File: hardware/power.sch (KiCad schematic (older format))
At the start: 14 parts

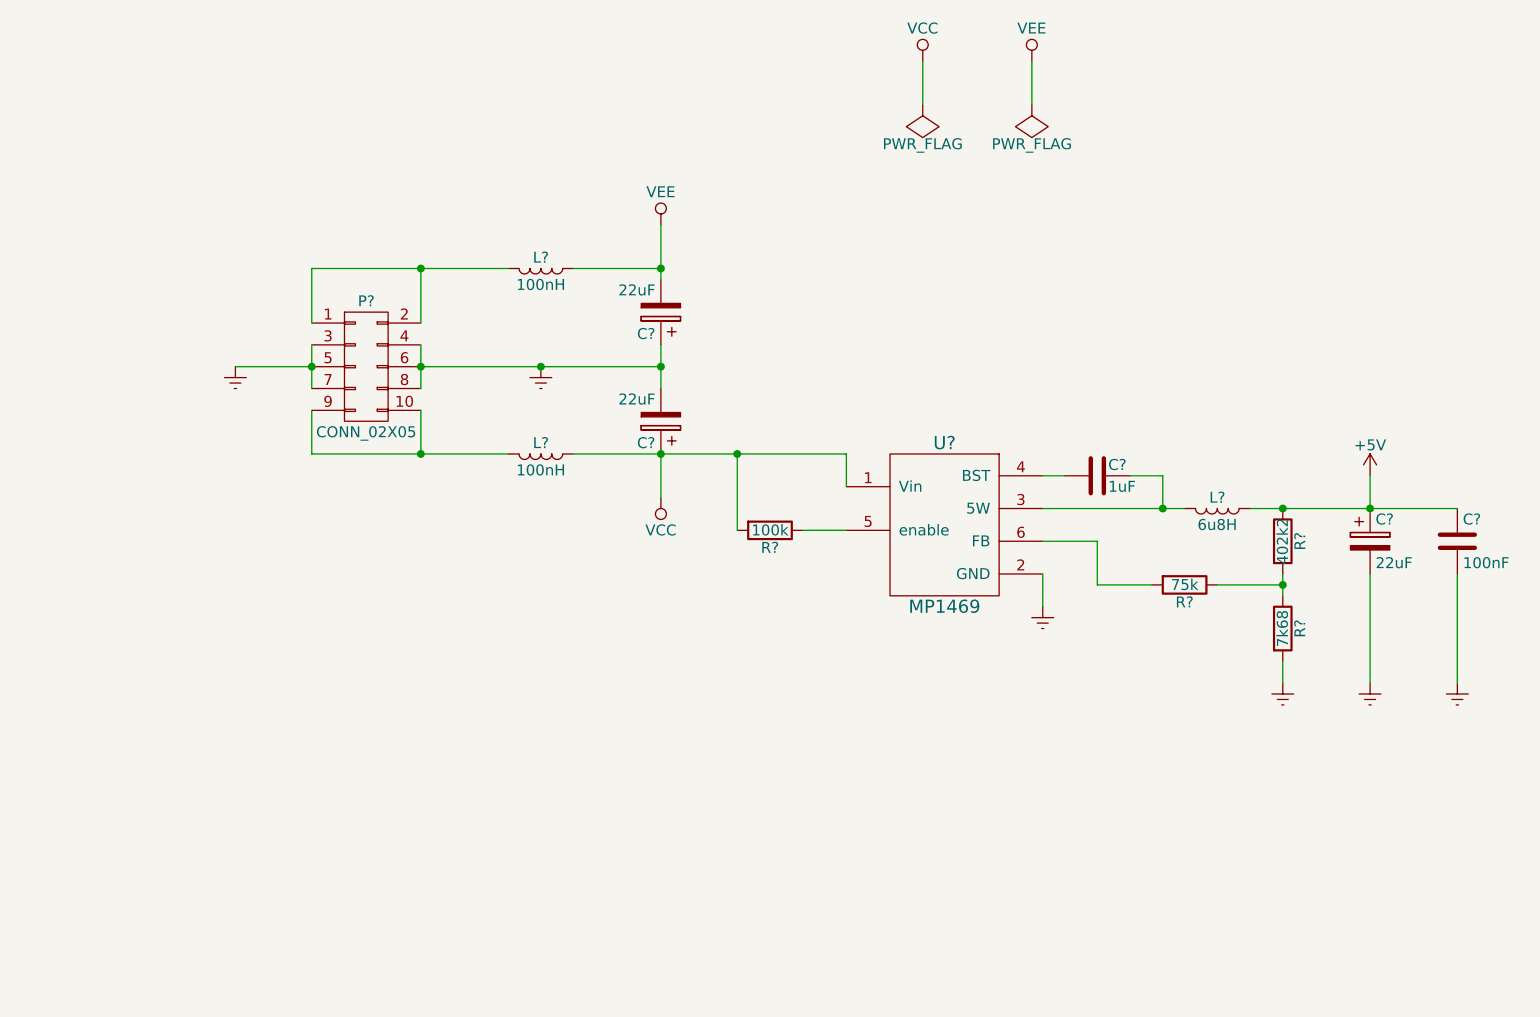
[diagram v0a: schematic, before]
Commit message: jacks on a different sheet than the buffers. single PCB with jumpers and mouse bites
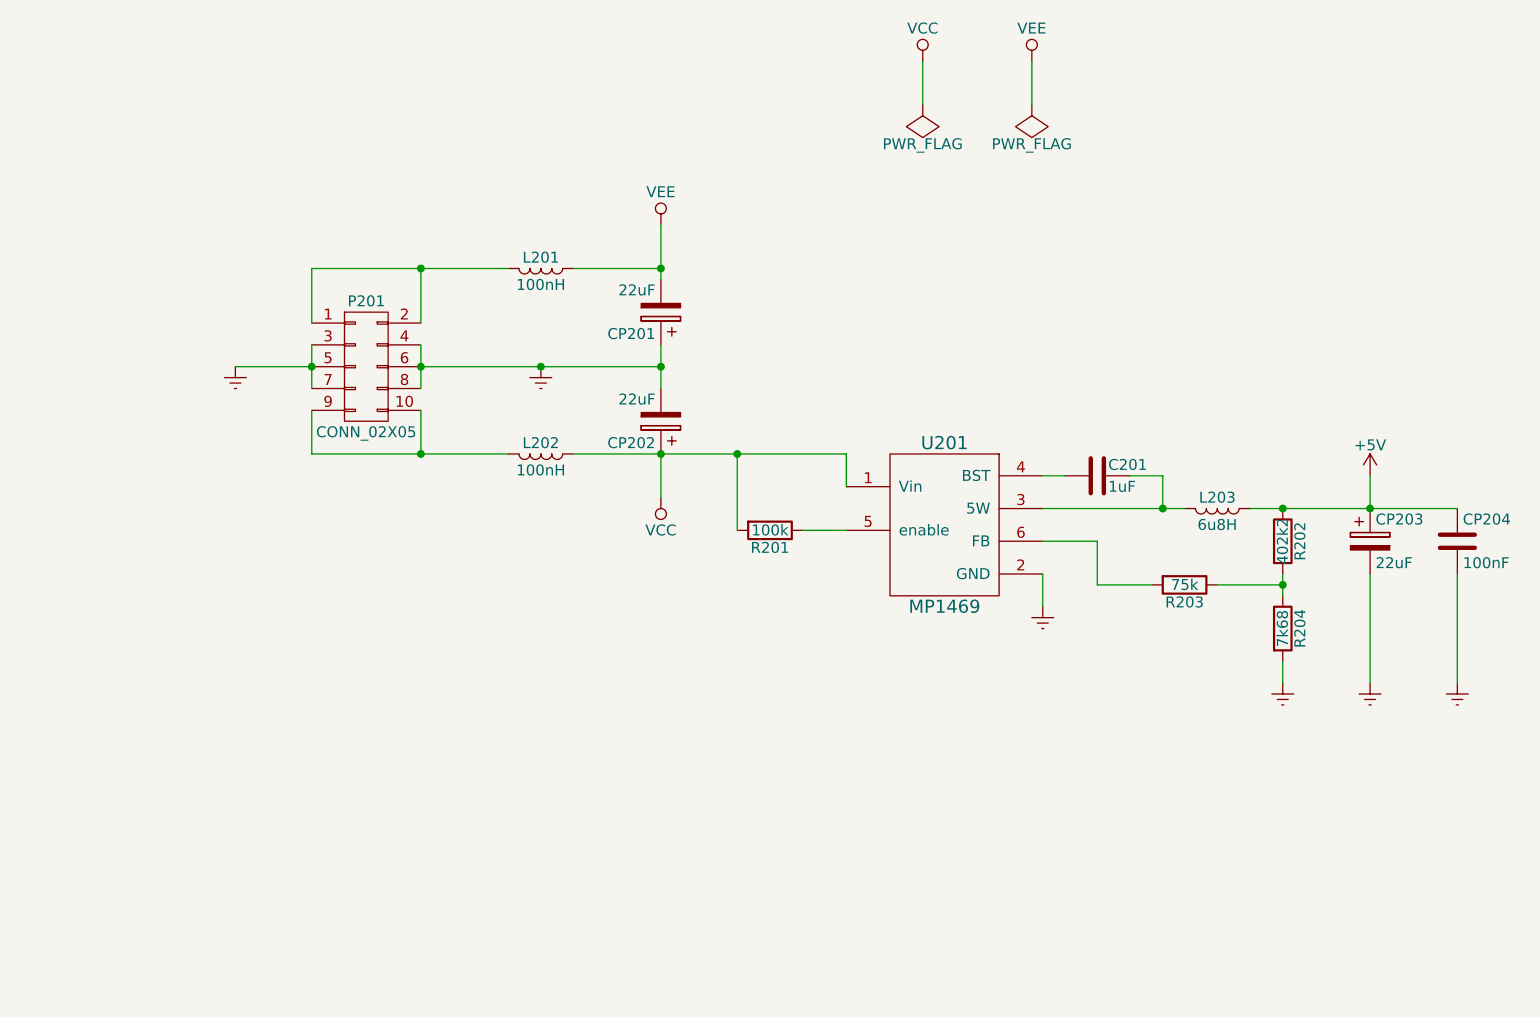
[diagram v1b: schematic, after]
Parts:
- gave numbers to parts that had none: 14
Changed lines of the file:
@@
 $Descr A4 11693 8268
 encoding utf-8
-Sheet 2 4
+Sheet 2 6
 Title ""
 Date ""
@@
 $EndDescr
 $Comp
-L CP C?
+L CP CP201
 U 1 1 5BE1E2D2
 P 4950 2250
-F 0 "C?" H 4975 2350 50  0000 L CNN
+F 0 "CP201" H 4975 2350 50  0000 L CNN
 F 1 "22uF" H 4975 2150 50  0000 L CNN
-F 2 "" H 4988 2100 50  0000 C CNN
+F 2 "" H 4988 2100 50  0001 C CNN
 F 3 "" H 4950 2250 50  0000 C CNN
 	1    4950 2250
@@
 $EndComp
 $Comp
-L CP C?
+L CP CP202
 U 1 1 5BE1E2F6
 P 4950 2750
-F 0 "C?" H 4975 2850 50  0000 L CNN
+F 0 "CP202" H 4975 2850 50  0000 L CNN
 F 1 "22uF" H 4975 2650 50  0000 L CNN
-F 2 "" H 4988 2600 50  0000 C CNN
+F 2 "" H 4988 2600 50  0001 C CNN
 F 3 "" H 4950 2750 50  0000 C CNN
 	1    4950 2750
@@
 $EndComp
 $Comp
-L R R?
+L R R201
 U 1 1 5BE1E3E6
 P 5450 3250
-F 0 "R?" V 5530 3250 50  0000 C CNN
+F 0 "R201" V 5530 3250 50  0000 C CNN
 F 1 "100k" V 5450 3250 50  0000 C CNN
-F 2 "" V 5380 3250 50  0000 C CNN
+F 2 "" V 5380 3250 50  0001 C CNN
 F 3 "" H 5450 3250 50  0000 C CNN
 	1    5450 3250
@@
 	4950 1850 4950 2100
 $Comp
-L L L?
+L L L201
 U 1 1 5BE1E5E0
 P 4400 2050
-F 0 "L?" V 4350 2050 50  0000 C CNN
+F 0 "L201" V 4350 2050 50  0000 C CNN
 F 1 "100nH" V 4475 2050 50  0000 C CNN
-F 2 "" H 4400 2050 50  0000 C CNN
+F 2 "" H 4400 2050 50  0001 C CNN
 F 3 "" H 4400 2050 50  0000 C CNN
 	1    4400 2050
@@
 $EndComp
 $Comp
-L L L?
+L L L202
 U 1 1 5BE1E717
 P 4400 2900
-F 0 "L?" V 4350 2900 50  0000 C CNN
+F 0 "L202" V 4350 2900 50  0000 C CNN
 F 1 "100nH" V 4475 2900 50  0000 C CNN
-F 2 "" H 4400 2900 50  0000 C CNN
+F 2 "" H 4400 2900 50  0001 C CNN
 F 3 "" H 4400 2900 50  0000 C CNN
 	1    4400 2900
@@
 	4550 2900 5800 2900
 $Comp
-L L L?
+L L L203
 U 1 1 5BE1E8D0
 P 7500 3150
-F 0 "L?" V 7450 3150 50  0000 C CNN
+F 0 "L203" V 7450 3150 50  0000 C CNN
 F 1 "6u8H" V 7575 3150 50  0000 C CNN
-F 2 "" H 7500 3150 50  0000 C CNN
+F 2 "" H 7500 3150 50  0001 C CNN
 F 3 "" H 7500 3150 50  0000 C CNN
 	1    7500 3150
@@
 $EndComp
 $Comp
-L MP1469 U?
+L MP1469 U201
 U 1 1 5BE1ECAF
 P 6250 3250
-F 0 "U?" H 6250 3650 60  0000 C CNN
+F 0 "U201" H 6250 3650 60  0000 C CNN
 F 1 "MP1469" H 6250 2900 60  0000 C CNN
 F 2 "" H 6100 3150 60  0001 C CNN
@@
 Connection ~ 5300 2900
 $Comp
-L C C?
+L C C201
 U 1 1 5BE1EF8F
 P 6950 3000
-F 0 "C?" V 6900 3050 50  0000 L CNN
+F 0 "C201" V 6900 3050 50  0000 L CNN
 F 1 "1uF" V 7000 3050 50  0000 L CNN
-F 2 "" H 6988 2850 50  0000 C CNN
+F 2 "" H 6988 2850 50  0001 C CNN
 F 3 "" H 6950 3000 50  0000 C CNN
 	1    6950 3000
@@
 	7100 3000 7250 3000
 $Comp
-L Earth #PWR?
+L Earth #PWR08
 U 1 1 5BE1F1F6
 P 6700 3600
-F 0 "#PWR?" H 6700 3350 50  0001 C CNN
+F 0 "#PWR08" H 6700 3350 50  0001 C CNN
 F 1 "Earth" H 6700 3450 50  0001 C CNN
 F 2 "" H 6700 3600 50  0000 C CNN
@@
 	6700 3450 6700 3600
 $Comp
-L R R?
+L R R203
 U 1 1 5BE1F26C
 P 7350 3500
-F 0 "R?" V 7430 3500 50  0000 C CNN
+F 0 "R203" V 7430 3500 50  0000 C CNN
 F 1 "75k" V 7350 3500 50  0000 C CNN
-F 2 "" V 7280 3500 50  0000 C CNN
+F 2 "" V 7280 3500 50  0001 C CNN
 F 3 "" H 7350 3500 50  0000 C CNN
 	1    7350 3500
@@
 	6700 3300 6950 3300
 $Comp
-L CP C?
+L CP CP203
 U 1 1 5BE1F3E4
 P 8200 3300
-F 0 "C?" H 8225 3400 50  0000 L CNN
+F 0 "CP203" H 8225 3400 50  0000 L CNN
 F 1 "22uF" H 8225 3200 50  0000 L CNN
-F 2 "" H 8238 3150 50  0000 C CNN
+F 2 "" H 8238 3150 50  0001 C CNN
 F 3 "" H 8200 3300 50  0000 C CNN
 	1    8200 3300
@@
 $EndComp
 $Comp
-L +5V #PWR?
+L +5V #PWR09
 U 1 1 5BE1F4C6
 P 8200 3000
-F 0 "#PWR?" H 8200 2850 50  0001 C CNN
+F 0 "#PWR09" H 8200 2850 50  0001 C CNN
 F 1 "+5V" H 8200 3140 50  0000 C CNN
 F 2 "" H 8200 3000 50  0000 C CNN
@@
 $EndComp
 $Comp
-L R R?
+L R R204
 U 1 1 5BE1F506
 P 7800 3700
-F 0 "R?" V 7880 3700 50  0000 C CNN
+F 0 "R204" V 7880 3700 50  0000 C CNN
 F 1 "7k68" V 7800 3700 50  0000 C CNN
-F 2 "" V 7730 3700 50  0000 C CNN
+F 2 "" V 7730 3700 50  0001 C CNN
 F 3 "" H 7800 3700 50  0000 C CNN
 	1    7800 3700
@@
 $EndComp
 $Comp
-L R R?
+L R R202
 U 1 1 5BE1F574
 P 7800 3300
-F 0 "R?" V 7880 3300 50  0000 C CNN
+F 0 "R202" V 7880 3300 50  0000 C CNN
 F 1 "402k2" V 7800 3300 50  0000 C CNN
-F 2 "" V 7730 3300 50  0000 C CNN
+F 2 "" V 7730 3300 50  0001 C CNN
 F 3 "" H 7800 3300 50  0000 C CNN
 	1    7800 3300
@@
 Connection ~ 8200 3150
 $Comp
-L C C?
+L C CP204
 U 1 1 5BE1F870
 P 8600 3300
-F 0 "C?" H 8625 3400 50  0000 L CNN
+F 0 "CP204" H 8625 3400 50  0000 L CNN
 F 1 "100nF" H 8625 3200 50  0000 L CNN
-F 2 "" H 8638 3150 50  0000 C CNN
+F 2 "" H 8638 3150 50  0001 C CNN
 F 3 "" H 8600 3300 50  0000 C CNN
 	1    8600 3300
@@
 $EndComp
 $Comp
-L Earth #PWR?
+L Earth #PWR010
 U 1 1 5BE1F909
 P 7800 3950
-F 0 "#PWR?" H 7800 3700 50  0001 C CNN
+F 0 "#PWR010" H 7800 3700 50  0001 C CNN
 F 1 "Earth" H 7800 3800 50  0001 C CNN
 F 2 "" H 7800 3950 50  0000 C CNN
@@
 $EndComp
 $Comp
-L Earth #PWR?
+L Earth #PWR011
 U 1 1 5BE1F942
 P 8200 3950
-F 0 "#PWR?" H 8200 3700 50  0001 C CNN
+F 0 "#PWR011" H 8200 3700 50  0001 C CNN
 F 1 "Earth" H 8200 3800 50  0001 C CNN
 F 2 "" H 8200 3950 50  0000 C CNN
@@
 $EndComp
 $Comp
-L Earth #PWR?
+L Earth #PWR012
 U 1 1 5BE1F974
 P 8600 3950
-F 0 "#PWR?" H 8600 3700 50  0001 C CNN
+F 0 "#PWR012" H 8600 3700 50  0001 C CNN
 F 1 "Earth" H 8600 3800 50  0001 C CNN
 F 2 "" H 8600 3950 50  0000 C CNN
@@
 	6950 3500 7200 3500
 $Comp
-L CONN_02X05 P?
+L CONN_02X05 P201
 U 1 1 5BE200D6
 P 3600 2500
-F 0 "P?" H 3600 2800 50  0000 C CNN
+F 0 "P201" H 3600 2800 50  0000 C CNN
 F 1 "CONN_02X05" H 3600 2200 50  0000 C CNN
-F 2 "" H 3600 1300 50  0000 C CNN
+F 2 "" H 3600 1300 50  0001 C CNN
 F 3 "" H 3600 1300 50  0000 C CNN
 	1    3600 2500
@@
 Connection ~ 3850 2500
 $Comp
-L Earth #PWR?
+L Earth #PWR013
 U 1 1 5BE20639
 P 4400 2500
-F 0 "#PWR?" H 4400 2250 50  0001 C CNN
+F 0 "#PWR013" H 4400 2250 50  0001 C CNN
 F 1 "Earth" H 4400 2350 50  0001 C CNN
 F 2 "" H 4400 2500 50  0000 C CNN
@@
 	3350 2500 3000 2500
 $Comp
-L Earth #PWR?
+L Earth #PWR014
 U 1 1 5BE20981
 P 3000 2500
-F 0 "#PWR?" H 3000 2250 50  0001 C CNN
+F 0 "#PWR014" H 3000 2250 50  0001 C CNN
 F 1 "Earth" H 3000 2350 50  0001 C CNN
 F 2 "" H 3000 2500 50  0000 C CNN
@@
 	4550 2050 4950 2050
 $Comp
-L VCC #PWR?
+L VCC #PWR015
 U 1 1 5BE23358
 P 4950 3100
-F 0 "#PWR?" H 4950 2950 50  0001 C CNN
+F 0 "#PWR015" H 4950 2950 50  0001 C CNN
 F 1 "VCC" H 4950 3250 50  0000 C CNN
 F 2 "" H 4950 3100 50  0000 C CNN
@@
 $EndComp
 $Comp
-L VEE #PWR?
+L VEE #PWR016
 U 1 1 5BE2338D
 P 4950 1850
-F 0 "#PWR?" H 4950 1700 50  0001 C CNN
+F 0 "#PWR016" H 4950 1700 50  0001 C CNN
 F 1 "VEE" H 4950 2000 50  0000 C CNN
 F 2 "" H 4950 1850 50  0000 C CNN
@@
 $EndComp
 $Comp
-L VCC #PWR?
+L VCC #PWR017
 U 1 1 5BE23935
 P 6150 1100
-F 0 "#PWR?" H 6150 950 50  0001 C CNN
+F 0 "#PWR017" H 6150 950 50  0001 C CNN
 F 1 "VCC" H 6150 1250 50  0000 C CNN
 F 2 "" H 6150 1100 50  0000 C CNN
@@
 $EndComp
 $Comp
-L PWR_FLAG #FLG?
+L PWR_FLAG #FLG018
 U 1 1 5BE23981
 P 6150 1300
-F 0 "#FLG?" H 6150 1395 50  0001 C CNN
+F 0 "#FLG018" H 6150 1395 50  0001 C CNN
 F 1 "PWR_FLAG" H 6150 1480 50  0000 C CNN
 F 2 "" H 6150 1300 50  0000 C CNN
@@
 $EndComp
 $Comp
-L VEE #PWR?
+L VEE #PWR019
 U 1 1 5BE239F7
 P 6650 1100
-F 0 "#PWR?" H 6650 950 50  0001 C CNN
+F 0 "#PWR019" H 6650 950 50  0001 C CNN
 F 1 "VEE" H 6650 1250 50  0000 C CNN
 F 2 "" H 6650 1100 50  0000 C CNN
@@
 $EndComp
 $Comp
-L PWR_FLAG #FLG?
+L PWR_FLAG #FLG020
 U 1 1 5BE23A33
 P 6650 1300
-F 0 "#FLG?" H 6650 1395 50  0001 C CNN
+F 0 "#FLG020" H 6650 1395 50  0001 C CNN
 F 1 "PWR_FLAG" H 6650 1480 50  0000 C CNN
 F 2 "" H 6650 1300 50  0000 C CNN

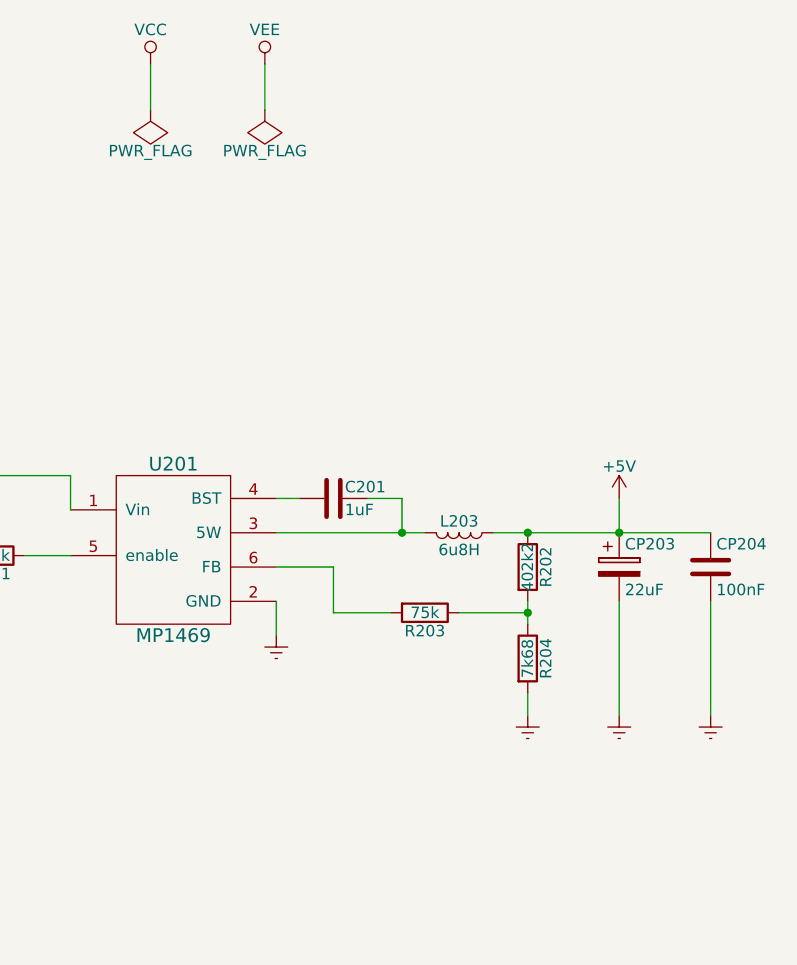
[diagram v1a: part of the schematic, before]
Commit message: most of the scematic is complete with the exception of the -5V offset
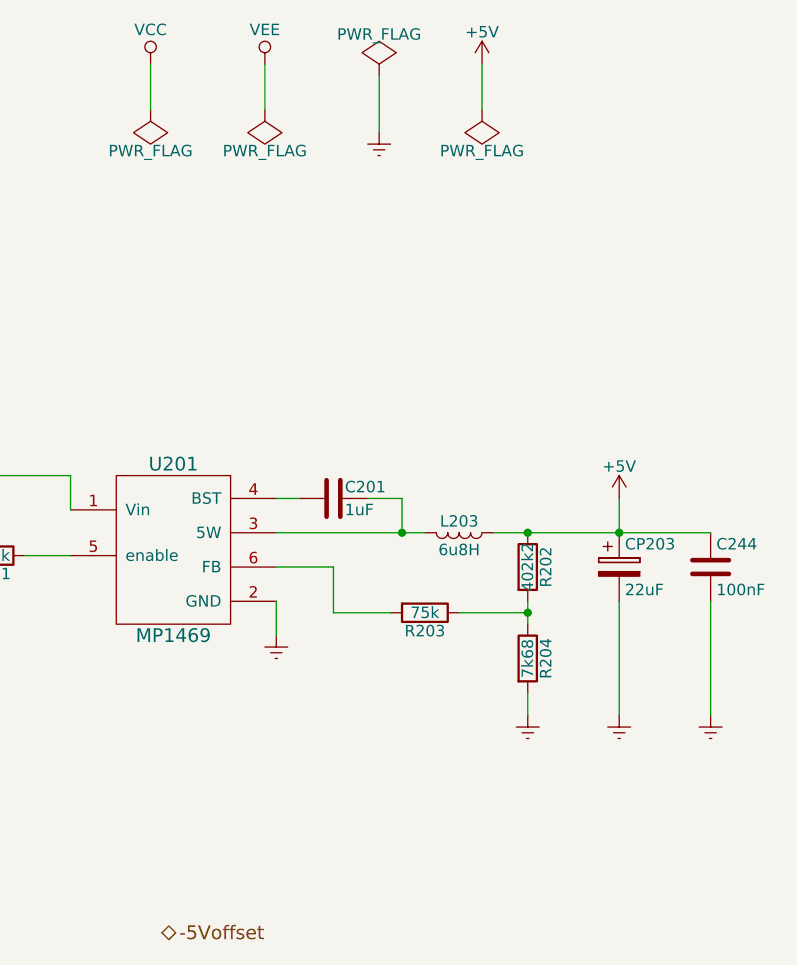
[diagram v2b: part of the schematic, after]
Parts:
- C201: footprint (none) -> Capacitors_THT:C_Rect_L11.5mm_W2.8mm_P10.00mm_MKT
- C244: renamed from CP204; footprint (none) -> Capacitors_THT:C_Axial_L5.1mm_D3.1mm_P7.50mm_Horizontal
- CP201, CP202, CP203: footprint (none) -> Capacitors_THT:CP_Radial_D10.0mm_P5.00mm
- L201, L202: footprint (none) -> Choke_SMD:Choke_Double_SMD_Wuerth-WE-DD-Typ-M-Typ-S
- L203: footprint (none) -> Choke_Toroid_ThroughHole:Choke_Toroid_horizontal_Diameter4-5mm_Amidon-T16
- P201: footprint (none) -> Connectors:IDC_Header_Straight_10pins
- R201, R202, R203, R204: footprint (none) -> Resistors_Universal:Resistor_SMD+THTuniversal_0805to1206_RM10_HandSoldering_RevA_Date25Jun2010
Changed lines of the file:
@@
 F 0 "CP201" H 4975 2350 50  0000 L CNN
 F 1 "22uF" H 4975 2150 50  0000 L CNN
-F 2 "" H 4988 2100 50  0001 C CNN
+F 2 "Capacitors_THT:CP_Radial_D10.0mm_P5.00mm" H 4988 2100 50  0001 C CNN
 F 3 "" H 4950 2250 50  0000 C CNN
 	1    4950 2250
@@
 F 0 "CP202" H 4975 2850 50  0000 L CNN
 F 1 "22uF" H 4975 2650 50  0000 L CNN
-F 2 "" H 4988 2600 50  0001 C CNN
+F 2 "Capacitors_THT:CP_Radial_D10.0mm_P5.00mm" H 4988 2600 50  0001 C CNN
 F 3 "" H 4950 2750 50  0000 C CNN
 	1    4950 2750
@@
 F 0 "R201" V 5530 3250 50  0000 C CNN
 F 1 "100k" V 5450 3250 50  0000 C CNN
-F 2 "" V 5380 3250 50  0001 C CNN
+F 2 "Resistors_Universal:Resistor_SMD+THTuniversal_0805to1206_RM10_HandSoldering_RevA_Date25Jun2010" V 5380 3250 50  0001 C CNN
 F 3 "" H 5450 3250 50  0000 C CNN
 	1    5450 3250
@@
 F 0 "L201" V 4350 2050 50  0000 C CNN
 F 1 "100nH" V 4475 2050 50  0000 C CNN
-F 2 "" H 4400 2050 50  0001 C CNN
+F 2 "Choke_SMD:Choke_Double_SMD_Wuerth-WE-DD-Typ-M-Typ-S" H 4400 2050 50  0001 C CNN
 F 3 "" H 4400 2050 50  0000 C CNN
 	1    4400 2050
@@
 F 0 "L202" V 4350 2900 50  0000 C CNN
 F 1 "100nH" V 4475 2900 50  0000 C CNN
-F 2 "" H 4400 2900 50  0001 C CNN
+F 2 "Choke_SMD:Choke_Double_SMD_Wuerth-WE-DD-Typ-M-Typ-S" H 4400 2900 50  0001 C CNN
 F 3 "" H 4400 2900 50  0000 C CNN
 	1    4400 2900
@@
 F 0 "L203" V 7450 3150 50  0000 C CNN
 F 1 "6u8H" V 7575 3150 50  0000 C CNN
-F 2 "" H 7500 3150 50  0001 C CNN
+F 2 "Choke_Toroid_ThroughHole:Choke_Toroid_horizontal_Diameter4-5mm_Amidon-T16" H 7500 3150 50  0001 C CNN
 F 3 "" H 7500 3150 50  0000 C CNN
 	1    7500 3150
@@
 F 0 "C201" V 6900 3050 50  0000 L CNN
 F 1 "1uF" V 7000 3050 50  0000 L CNN
-F 2 "" H 6988 2850 50  0001 C CNN
+F 2 "Capacitors_THT:C_Rect_L11.5mm_W2.8mm_P10.00mm_MKT" H 6988 2850 50  0001 C CNN
 F 3 "" H 6950 3000 50  0000 C CNN
 	1    6950 3000
@@
 F 0 "R203" V 7430 3500 50  0000 C CNN
 F 1 "75k" V 7350 3500 50  0000 C CNN
-F 2 "" V 7280 3500 50  0001 C CNN
+F 2 "Resistors_Universal:Resistor_SMD+THTuniversal_0805to1206_RM10_HandSoldering_RevA_Date25Jun2010" V 7280 3500 50  0001 C CNN
 F 3 "" H 7350 3500 50  0000 C CNN
 	1    7350 3500
@@
 F 0 "CP203" H 8225 3400 50  0000 L CNN
 F 1 "22uF" H 8225 3200 50  0000 L CNN
-F 2 "" H 8238 3150 50  0001 C CNN
+F 2 "Capacitors_THT:CP_Radial_D10.0mm_P5.00mm" H 8238 3150 50  0001 C CNN
 F 3 "" H 8200 3300 50  0000 C CNN
 	1    8200 3300
@@
 F 0 "R204" V 7880 3700 50  0000 C CNN
 F 1 "7k68" V 7800 3700 50  0000 C CNN
-F 2 "" V 7730 3700 50  0001 C CNN
+F 2 "Resistors_Universal:Resistor_SMD+THTuniversal_0805to1206_RM10_HandSoldering_RevA_Date25Jun2010" V 7730 3700 50  0001 C CNN
 F 3 "" H 7800 3700 50  0000 C CNN
 	1    7800 3700
@@
 F 0 "R202" V 7880 3300 50  0000 C CNN
 F 1 "402k2" V 7800 3300 50  0000 C CNN
-F 2 "" V 7730 3300 50  0001 C CNN
+F 2 "Resistors_Universal:Resistor_SMD+THTuniversal_0805to1206_RM10_HandSoldering_RevA_Date25Jun2010" V 7730 3300 50  0001 C CNN
 F 3 "" H 7800 3300 50  0000 C CNN
 	1    7800 3300
@@
 Connection ~ 8200 3150
 $Comp
-L C CP204
+L C C244
 U 1 1 5BE1F870
 P 8600 3300
-F 0 "CP204" H 8625 3400 50  0000 L CNN
+F 0 "C244" H 8625 3400 50  0000 L CNN
 F 1 "100nF" H 8625 3200 50  0000 L CNN
-F 2 "" H 8638 3150 50  0001 C CNN
+F 2 "Capacitors_THT:C_Axial_L5.1mm_D3.1mm_P7.50mm_Horizontal" H 8638 3150 50  0001 C CNN
 F 3 "" H 8600 3300 50  0000 C CNN
 	1    8600 3300
@@
 F 0 "P201" H 3600 2800 50  0000 C CNN
 F 1 "CONN_02X05" H 3600 2200 50  0000 C CNN
-F 2 "" H 3600 1300 50  0001 C CNN
+F 2 "Connectors:IDC_Header_Straight_10pins" H 3600 1300 50  0001 C CNN
 F 3 "" H 3600 1300 50  0000 C CNN
 	1    3600 2500
@@
 Wire Wire Line
 	6650 1100 6650 1300
+Text HLabel 6200 4900 2    60   BiDi ~ 0
+-5Voffset
+$Comp
+L PWR_FLAG #FLG021
+U 1 1 5BE69751
+P 7150 1150
+F 0 "#FLG021" H 7150 1245 50  0001 C CNN
+F 1 "PWR_FLAG" H 7150 1330 50  0000 C CNN
+F 2 "" H 7150 1150 50  0000 C CNN
+F 3 "" H 7150 1150 50  0000 C CNN
+	1    7150 1150
+	1    0    0    -1
+$EndComp
+$Comp
+L Earth #PWR022
+U 1 1 5BE69788
+P 7150 1400
+F 0 "#PWR022" H 7150 1150 50  0001 C CNN
+F 1 "Earth" H 7150 1250 50  0001 C CNN
+F 2 "" H 7150 1400 50  0000 C CNN
+F 3 "" H 7150 1400 50  0000 C CNN
+	1    7150 1400
+	1    0    0    -1
+$EndComp
+Wire Wire Line
+	7150 1150 7150 1400
+$Comp
+L +5V #PWR023
+U 1 1 5BE69E73
+P 7600 1100
+F 0 "#PWR023" H 7600 950 50  0001 C CNN
+F 1 "+5V" H 7600 1240 50  0000 C CNN
+F 2 "" H 7600 1100 50  0000 C CNN
+F 3 "" H 7600 1100 50  0000 C CNN
+	1    7600 1100
+	1    0    0    -1
+$EndComp
+$Comp
+L PWR_FLAG #FLG024
+U 1 1 5BE69EA8
+P 7600 1300
+F 0 "#FLG024" H 7600 1395 50  0001 C CNN
+F 1 "PWR_FLAG" H 7600 1480 50  0000 C CNN
+F 2 "" H 7600 1300 50  0000 C CNN
+F 3 "" H 7600 1300 50  0000 C CNN
+	1    7600 1300
+	-1   0    0    1
+$EndComp
+Wire Wire Line
+	7600 1300 7600 1100
 $EndSCHEMATC
